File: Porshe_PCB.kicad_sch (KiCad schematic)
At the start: 35 parts, among them IC1 RASPBERRY_PI_PICO_W, J1 Conn_01x04_Socket, J10 Conn_01x03_Socket, J11 Conn_01x04_Socket, J12 Conn_01x01_Pin, J2 SM04B-SRSS-TB_LF__SN_, J3 Conn_01x04_Socket, J4 S2B-PH-SM4-TB_LF__SN_, J5 Screw_Terminal_01x03, J6 Conn_01x01_Pin, J7 Conn_01x01_Pin, J8 Conn_01x01_Pin, Q1 DMG2305UX-7, U1 DS3231SN, U2 AHT20

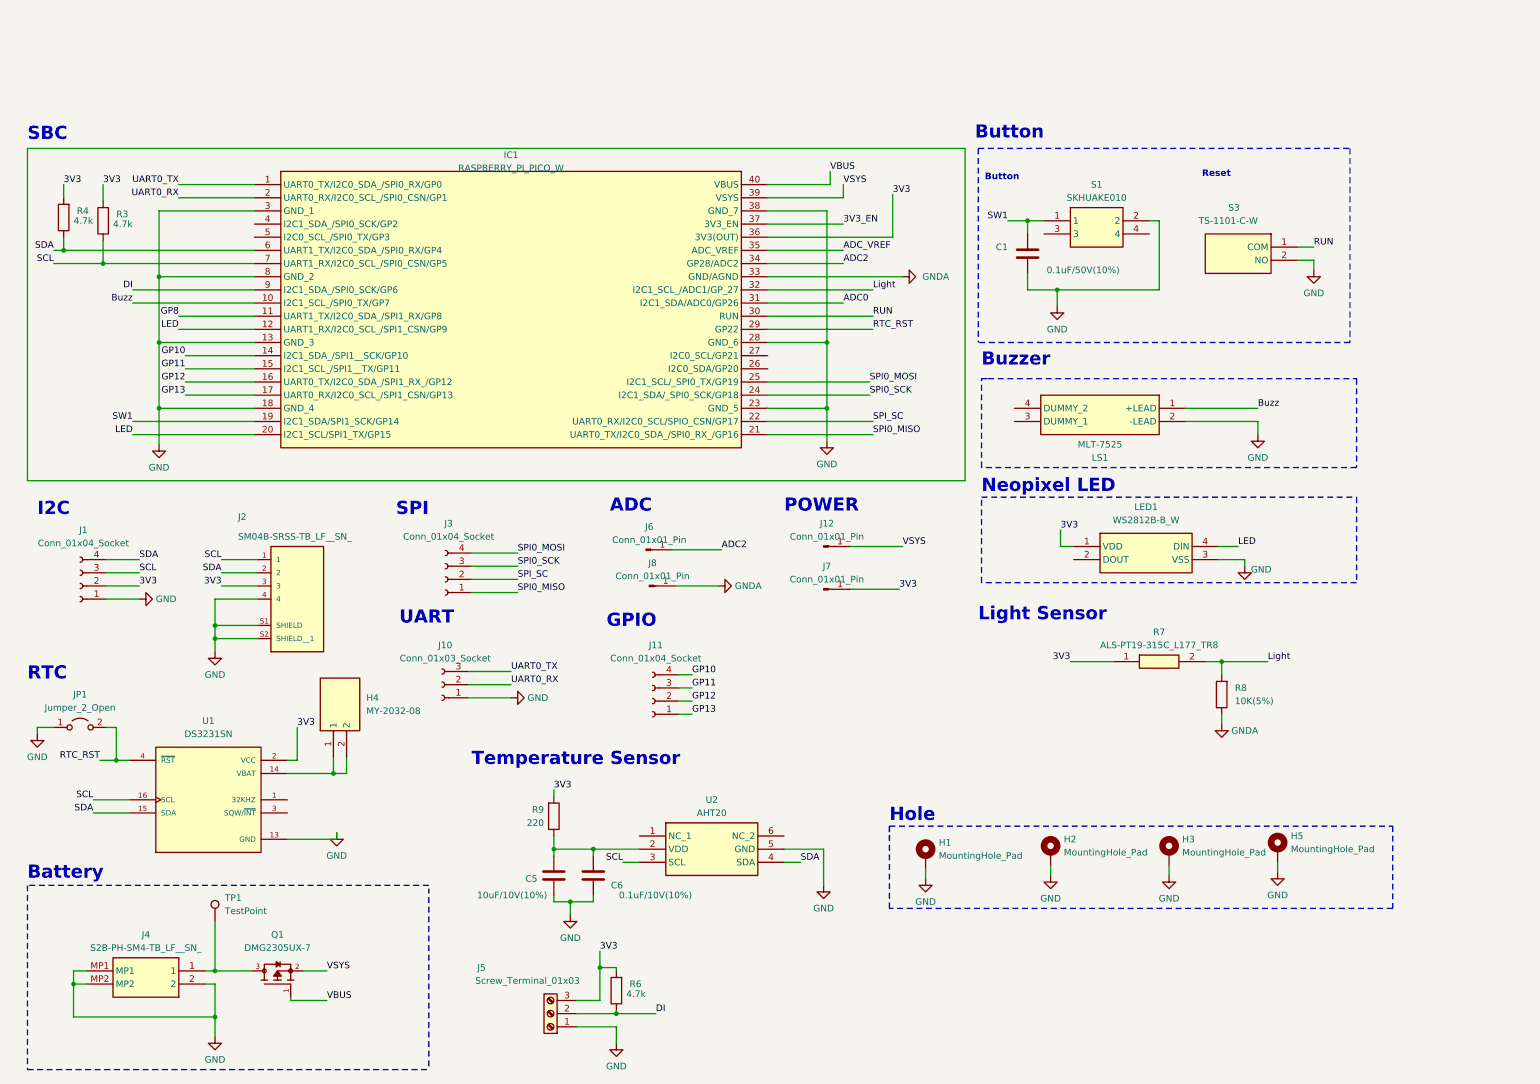
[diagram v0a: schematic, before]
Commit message: 코인베터리 접지추가
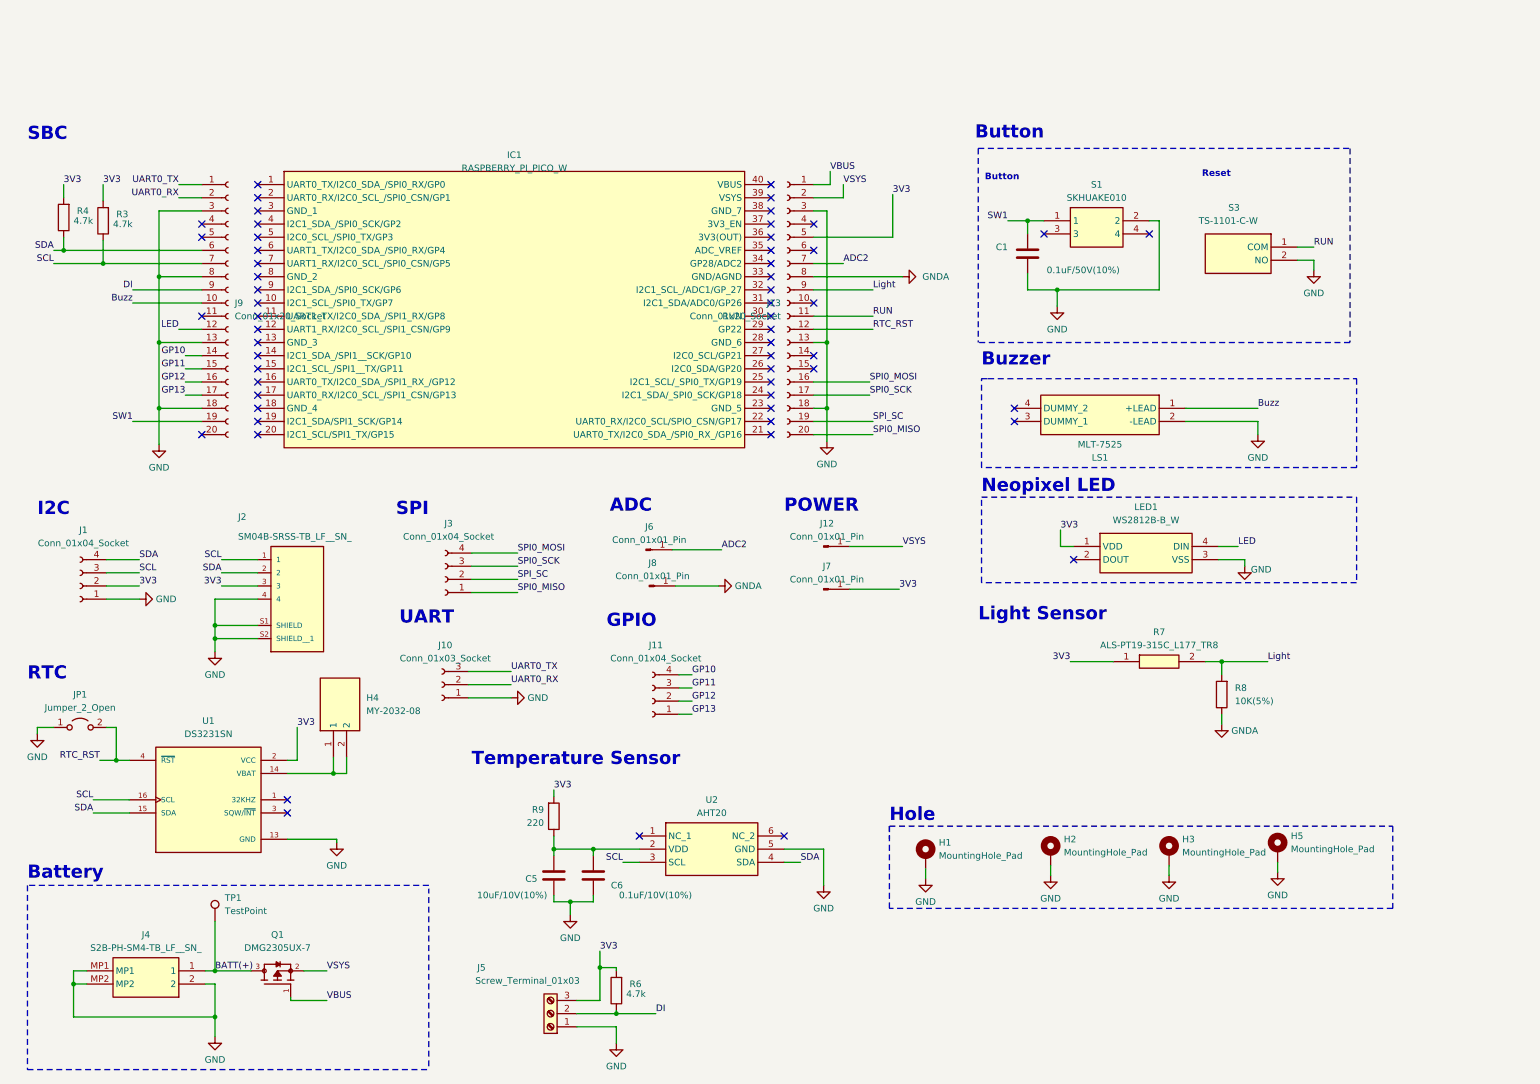
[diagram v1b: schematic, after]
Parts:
- added J13: Conn_01x20_Socket, Connector_PinSocket_2.54mm:PinSocket_1x20_P2.54mm_Vertical_SMD_Pin1Right, symbol Connector:Conn_01x20_Socket
- added J9: Conn_01x20_Socket, Connector_PinSocket_2.54mm:PinSocket_1x20_P2.54mm_Vertical_SMD_Pin1Left, symbol Connector:Conn_01x20_Socket
- IC1: now left out of the parts list
- J1, J11: footprint Connector_PinHeader_2.54mm:PinHeader_1x04_P2.54mm_Vertical -> (none)
- J3: footprint Connector_PinHeader_2.54mm:PinHeader_1x04_P2.54mm_Vertical -> Connector_PinSocket_2.54mm:PinSocket_1x04_P2.54mm_Vertical
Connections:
- net 3V3: now also J13.5 (Pin_5); no longer IC1.36 (3V3(OUT))
- net ADC2: now also J13.7 (Pin_7); no longer IC1.34 (GP28/ADC2)
- net Buzz: now also J9.10 (Pin_10); no longer IC1.10 (I2C1_SCL_/SPI0_TX/GP7)
- net DI: now also J9.9 (Pin_9); no longer IC1.9 (I2C1_SDA_/SPI0_SCK/GP6)
- net GND: now also J13.13 (Pin_13), J13.18 (Pin_18), J13.3 (Pin_3), J9.13 (Pin_13), J9.18 (Pin_18), J9.3 (Pin_3), J9.8 (Pin_8); no longer IC1.13 (GND_3), IC1.18 (GND_4), IC1.23 (GND_5), IC1.28 (GND_6), IC1.3 (GND_1), IC1.38 (GND_7), IC1.8 (GND_2)
- net GNDA: now also J13.8 (Pin_8); no longer IC1.33 (GND/AGND)
- net GP10: now also J9.14 (Pin_14); no longer IC1.14 (I2C1_SDA_/SPI1__SCK/GP10)
- net GP11: now also J9.15 (Pin_15); no longer IC1.15 (I2C1_SCL_/SPI1__TX/GP11)
- net GP12: now also J9.16 (Pin_16); no longer IC1.16 (UART0_TX/I2C0_SDA_/SPI1_RX_/GP12)
- net GP13: now also J9.17 (Pin_17); no longer IC1.17 (UART0_RX/I2C0_SCL_/SPI1_CSN/GP13)
- net LED: now also J9.12 (Pin_12); no longer IC1.12 (UART1_RX/I2C0_SCL_/SPI1_CSN/GP9), IC1.20 (I2C1_SCL/SPI1_TX/GP15)
- net Light: now also J13.9 (Pin_9); no longer IC1.32 (I2C1_SCL_/ADC1/GP_27)
- net RTC_RST: now also J13.12 (Pin_12); no longer IC1.29 (GP22)
- net RUN: now also J13.11 (Pin_11); no longer IC1.30 (RUN)
- net SCL: now also J9.7 (Pin_7); no longer IC1.7 (UART1_RX/I2C0_SCL_/SPI0_CSN/GP5)
- net SDA: now also J9.6 (Pin_6); no longer IC1.6 (UART1_TX/I2C0_SDA_/SPI0_RX/GP4)
- net SPI0_MISO: now also J13.20 (Pin_20); no longer IC1.21 (UART0_TX/I2C0_SDA_/SPI0_RX_/GP16)
- net SPI0_MOSI: now also J13.16 (Pin_16); no longer IC1.25 (I2C1_SCL/_SPI0_TX/GP19)
- net SPI0_SCK: now also J13.17 (Pin_17); no longer IC1.24 (I2C1_SDA/_SPI0_SCK/GP18)
- net SPI_SC: now also J13.19 (Pin_19); no longer IC1.22 (UART0_RX/I2C0_SCL/SPIO_CSN/GP17)
- net SW1: now also J9.19 (Pin_19); no longer IC1.19 (I2C1_SDA/SPI1_SCK/GP14)
- net UART0_RX: now also J9.2 (Pin_2); no longer IC1.2 (UART0_RX/I2C0_SCL_/SPI0_CSN/GP1)
- net UART0_TX: now also J9.1 (Pin_1); no longer IC1.1 (UART0_TX/I2C0_SDA_/SPI0_RX/GP0)
- net VBUS: now also J13.1 (Pin_1); no longer IC1.40 (VBUS)
- net VSYS: now also J13.2 (Pin_2); no longer IC1.39 (VSYS)
- net BATT(+): now reaches J4.1, Q1.3, TP1.1
- net 3V3_EN: no longer names the net of IC1.37 (3V3_EN)
- net ADC0: no longer names the net of IC1.31 (I2C1_SDA/ADC0/GP26)
- net ADC_VREF: no longer names the net of IC1.35 (ADC_VREF)
- net GP8: no longer names the net of IC1.11 (UART1_TX/I2C0_SDA_/SPI1_RX/GP8)
- no-connect marks 0 -> 58
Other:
- moved on the sheet: IC1

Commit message: 오토라우팅완료
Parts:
- J6, J7, J8: footprint Connector_Pin:Pin_D1.2mm_L10.2mm_W2.9mm_FlatFork -> Connector_Pin:Pin_D1.3mm_L11.0mm
- TP1: footprint TestPoint:TestPoint_Pad_D2.0mm -> TestPoint:TestPoint_Pad_D1.0mm
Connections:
- net 3V3: now also J8.1 (Pin_1); no longer J7.1 (Pin_1)
- net GNDA: now also J7.1 (Pin_1); no longer J8.1 (Pin_1)
- net BAK_VBAT: now reaches H4.1, H4.2, U1.14 (VBAT)
- net BATT(+) renamed VBAT(+)
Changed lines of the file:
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@@
     (effects (font (size 1.27 1.27)) (justify left bottom))
   )
-  (label "BATT(+)" (at 50.165 177.165 0) (fields_autoplaced)
+  (label "VBAT(+)" (at 50.165 177.165 0) (fields_autoplaced)
     (effects (font (size 1.27 1.27)) (justify left bottom))
   )
@@
   )
   (label "3V3" (at 213.36 92.075 0) (fields_autoplaced)
+    (effects (font (size 1.27 1.27)) (justify left bottom))
+  )
+  (label "BAK_VBAT" (at 64.77 139.065 0) (fields_autoplaced)
     (effects (font (size 1.27 1.27)) (justify left bottom))
   )
@@
     )
   )
+  (symbol (lib_id "Connector:Conn_01x01_Pin") (at 167.64 103.505 0) (unit 1)
+    (in_bom yes) (on_board yes) (dnp no) (fields_autoplaced)
+    (property "Reference" "J8" (at 168.275 99.06 0)
+      (effects (font (size 1.27 1.27)))
+    )
+    (property "Value" "Conn_01x01_Pin" (at 168.275 101.6 0)
+      (effects (font (size 1.27 1.27)))
+    )
+    (property "Footprint" "Connector_Pin:Pin_D1.3mm_L11.0mm" (at 167.64 103.505 0)
+      (effects (font (size 1.27 1.27)) hide)
+    )
+    (property "Datasheet" "~" (at 167.64 103.505 0)
+      (effects (font (size 1.27 1.27)) hide)
+    )
+    (property "Customfield" "" (at 167.64 103.505 0)
+      (effects (font (size 1.27 1.27)) hide)
+    )
+    (pin "1")
+    (instances
+      (project "Porshe_PCB"
+        (path "/8e8c2c0a-bd1c-4d8a-8f53-91cb65b3d33b"
+          (reference "J8") (unit 1)
+        )
+      )
+    )
+  )
   (symbol (lib_id "Connector:Conn_01x04_Socket") (at 134.62 125.095 180) (unit 1)
     (in_bom yes) (on_board yes) (dnp no) (fields_autoplaced)
@@
     )
   )
-  (symbol (lib_id "Connector:Conn_01x01_Pin") (at 167.64 103.505 0) (unit 1)
-    (in_bom yes) (on_board yes) (dnp no) (fields_autoplaced)
-    (property "Reference" "J7" (at 168.275 99.06 0)
-      (effects (font (size 1.27 1.27)))
-    )
-    (property "Value" "Conn_01x01_Pin" (at 168.275 101.6 0)
-      (effects (font (size 1.27 1.27)))
-    )
-    (property "Footprint" "Connector_Pin:Pin_D1.2mm_L10.2mm_W2.9mm_FlatFork" (at 167.64 103.505 0)
-      (effects (font (size 1.27 1.27)) hide)
-    )
-    (property "Datasheet" "~" (at 167.64 103.505 0)
-      (effects (font (size 1.27 1.27)) hide)
-    )
-    (property "Customfield" "" (at 167.64 103.505 0)
-      (effects (font (size 1.27 1.27)) hide)
-    )
-    (pin "1")
-    (instances
-      (project "Porshe_PCB"
-        (path "/8e8c2c0a-bd1c-4d8a-8f53-91cb65b3d33b"
-          (reference "J7") (unit 1)
-        )
-      )
-    )
-  )
   (symbol (lib_id "power:GNDA") (at 182.88 43.18 90) (unit 1)
     (in_bom yes) (on_board yes) (dnp no) (fields_autoplaced)
@@
         (path "/8e8c2c0a-bd1c-4d8a-8f53-91cb65b3d33b"
           (reference "#PWR021") (unit 1)
-        )
-      )
-    )
-  )
-  (symbol (lib_id "Connector:Conn_01x01_Pin") (at 133.985 102.87 0) (unit 1)
-    (in_bom yes) (on_board yes) (dnp no) (fields_autoplaced)
-    (property "Reference" "J8" (at 134.62 98.425 0)
-      (effects (font (size 1.27 1.27)))
-    )
-    (property "Value" "Conn_01x01_Pin" (at 134.62 100.965 0)
-      (effects (font (size 1.27 1.27)))
-    )
-    (property "Footprint" "Connector_Pin:Pin_D1.2mm_L10.2mm_W2.9mm_FlatFork" (at 133.985 102.87 0)
-      (effects (font (size 1.27 1.27)) hide)
-    )
-    (property "Datasheet" "~" (at 133.985 102.87 0)
-      (effects (font (size 1.27 1.27)) hide)
-    )
-    (property "Customfield" "" (at 133.985 102.87 0)
-      (effects (font (size 1.27 1.27)) hide)
-    )
-    (pin "1")
-    (instances
-      (project "Porshe_PCB"
-        (path "/8e8c2c0a-bd1c-4d8a-8f53-91cb65b3d33b"
-          (reference "J8") (unit 1)
         )
       )
@@
       (effects (font (size 1.27 1.27)))
     )
-    (property "Footprint" "Connector_Pin:Pin_D1.2mm_L10.2mm_W2.9mm_FlatFork" (at 133.35 95.885 0)
+    (property "Footprint" "Connector_Pin:Pin_D1.3mm_L11.0mm" (at 133.35 95.885 0)
       (effects (font (size 1.27 1.27)) hide)
     )
@@
       (effects (font (size 1.27 1.27)) (justify left))
     )
-    (property "Footprint" "TestPoint:TestPoint_Pad_D2.0mm" (at 55.245 167.64 0)
+    (property "Footprint" "TestPoint:TestPoint_Pad_D1.0mm" (at 55.245 167.64 0)
       (effects (font (size 1.27 1.27)) hide)
     )
@@
         )
       )
+    )
+  )
+  (symbol (lib_id "Connector:Conn_01x01_Pin") (at 133.985 102.87 0) (unit 1)
+    (in_bom yes) (on_board yes) (dnp no) (fields_autoplaced)
+    (property "Reference" "J7" (at 134.62 98.425 0)
+      (effects (font (size 1.27 1.27)))
+    )
+    (property "Value" "Conn_01x01_Pin" (at 134.62 100.965 0)
+      (effects (font (size 1.27 1.27)))
+    )
+    (property "Footprint" "Connector_Pin:Pin_D1.3mm_L11.0mm" (at 133.985 102.87 0)
+      (effects (font (size 1.27 1.27)) hide)
+    )
+    (property "Datasheet" "~" (at 133.985 102.87 0)
+      (effects (font (size 1.27 1.27)) hide)
+    )
+    (property "Customfield" "" (at 133.985 102.87 0)
+      (effects (font (size 1.27 1.27)) hide)
+    )
+    (pin "1")
+    (instances
+      (project "Porshe_PCB"
+        (path "/8e8c2c0a-bd1c-4d8a-8f53-91cb65b3d33b"
+          (reference "J7") (unit 1)
+        )
+      )
